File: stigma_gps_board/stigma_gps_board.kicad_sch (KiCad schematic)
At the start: 22 parts, among them J1 Conn_02x05_Top_Bottom, U1 NCP115AMX120TCG, U2 SAM-M10Q

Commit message: added 3d models and datasheets
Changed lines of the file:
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@@
 (kicad_sch
-	(version 20231120)
+	(version 20250114)
 	(generator "eeschema")
-	(generator_version "8.0")
+	(generator_version "9.0")
 	(paper "A4")
+	(rectangle
+		(start 128.27 59.69)
+		(end 189.23 95.25)
+		(stroke
+			(width 0)
+			(type default)
+		)
+		(fill
+			(type none)
+		)
+	)
+	(rectangle
+		(start 128.27 17.78)
+		(end 189.23 53.34)
+		(stroke
+			(width 0)
+			(type default)
+		)
+		(fill
+			(type none)
+		)
+	)
+	(rectangle
+		(start 128.27 99.06)
+		(end 189.23 132.08)
+		(stroke
+			(width 0)
+			(type default)
+		)
+		(fill
+			(type none)
+		)
+	)
+	(rectangle
+		(start 19.05 59.69)
+		(end 124.46 104.14)
+		(stroke
+			(width 0)
+			(type default)
+		)
+		(fill
+			(type none)
+		)
+	)
+	(rectangle
+		(start 19.05 17.78)
+		(end 124.46 53.34)
+		(stroke
+			(width 0)
+			(type default)
+		)
+		(fill
+			(type none)
+		)
+	)
+	(text "13mA should be the max. \nneeded current"
+		(exclude_from_sim no)
+		(at 110.998 101.092 0)
+		(effects
+			(font
+				(size 1.27 1.27)
+			)
+		)
+	)
+	(text "recomended chip setup"
+		(exclude_from_sim no)
+		(at 30.226 58.674 0)
+		(effects
+			(font
+				(size 1.27 1.27)
+			)
+		)
+	)
+	(text "connector and esd protection"
+		(exclude_from_sim no)
+		(at 33.274 16.51 0)
+		(effects
+			(font
+				(size 1.27 1.27)
+			)
+		)
+	)
+	(text "for more information about how to integrage refer to following:\nhttps://www.u-blox.com/en/product/sam-m10q-module?legacy=Current#Documentation-&-resources"
+		(exclude_from_sim no)
+		(at 19.05 107.188 0)
+		(effects
+			(font
+				(size 1.27 1.27)
+			)
+			(justify left)
+		)
+	)
+	(text "power supply\n"
+		(exclude_from_sim no)
+		(at 128.016 16.51 0)
+		(effects
+			(font
+				(size 1.27 1.27)
+			)
+			(justify left)
+		)
+	)
+	(text "todo: add footprint for connector (copy from stigma?)\n"
+		(exclude_from_sim no)
+		(at 47.244 55.372 0)
+		(effects
+			(font
+				(size 1.27 1.27)
+			)
+		)
+	)
+	(text "mounting hole m2"
+		(exclude_from_sim no)
+		(at 136.906 58.42 0)
+		(effects
+			(font
+				(size 1.27 1.27)
+			)
+		)
+	)
+	(text "mounting hole m4"
+		(exclude_from_sim no)
+		(at 136.906 98.044 0)
+		(effects
+			(font
+				(size 1.27 1.27)
+			)
+		)
+	)
 	(junction
 		(at 73.66 36.83)
@@
 		)
 	)
-	(rectangle
-		(start 128.27 59.69)
-		(end 189.23 95.25)
-		(stroke
-			(width 0)
-			(type default)
-		)
-		(fill
-			(type none)
-		)
-	)
-	(rectangle
-		(start 128.27 17.78)
-		(end 189.23 53.34)
-		(stroke
-			(width 0)
-			(type default)
-		)
-		(fill
-			(type none)
-		)
-	)
-	(rectangle
-		(start 128.27 99.06)
-		(end 189.23 132.08)
-		(stroke
-			(width 0)
-			(type default)
-		)
-		(fill
-			(type none)
-		)
-	)
-	(rectangle
-		(start 19.05 59.69)
-		(end 124.46 104.14)
-		(stroke
-			(width 0)
-			(type default)
-		)
-		(fill
-			(type none)
-		)
-	)
-	(rectangle
-		(start 19.05 17.78)
-		(end 124.46 53.34)
-		(stroke
-			(width 0)
-			(type default)
-		)
-		(fill
-			(type none)
-		)
-	)
-	(text "13mA should be the max. \nneeded current"
-		(exclude_from_sim no)
-		(at 110.998 101.092 0)
-		(effects
-			(font
-				(size 1.27 1.27)
-			)
-		)
-	)
-	(text "recomended chip setup"
-		(exclude_from_sim no)
-		(at 30.226 58.674 0)
-		(effects
-			(font
-				(size 1.27 1.27)
-			)
-		)
-	)
-	(text "connector and esd protection"
-		(exclude_from_sim no)
-		(at 33.274 16.51 0)
-		(effects
-			(font
-				(size 1.27 1.27)
-			)
-		)
-	)
-	(text "for more information about how to integrage refer to following:\nhttps://www.u-blox.com/en/product/sam-m10q-module?legacy=Current#Documentation-&-resources"
-		(exclude_from_sim no)
-		(at 19.05 107.188 0)
-		(effects
-			(font
-				(size 1.27 1.27)
-			)
-			(justify left)
-		)
-	)
-	(text "power supply\n"
-		(exclude_from_sim no)
-		(at 128.016 16.51 0)
-		(effects
-			(font
-				(size 1.27 1.27)
-			)
-			(justify left)
-		)
-	)
-	(text "todo: add footprint for connector (copy from stigma?)\n"
-		(exclude_from_sim no)
-		(at 47.244 55.372 0)
-		(effects
-			(font
-				(size 1.27 1.27)
-			)
-		)
-	)
-	(text "mounting hole m2"
-		(exclude_from_sim no)
-		(at 136.906 58.42 0)
-		(effects
-			(font
-				(size 1.27 1.27)
-			)
-		)
-	)
-	(text "mounting hole m4"
-		(exclude_from_sim no)
-		(at 136.906 98.044 0)
-		(effects
-			(font
-				(size 1.27 1.27)
-			)
-		)
-	)
 	(global_label "GPS_RESET"
 		(shape input)
@@
 		)
 	)
+	(embedded_fonts no)
 )

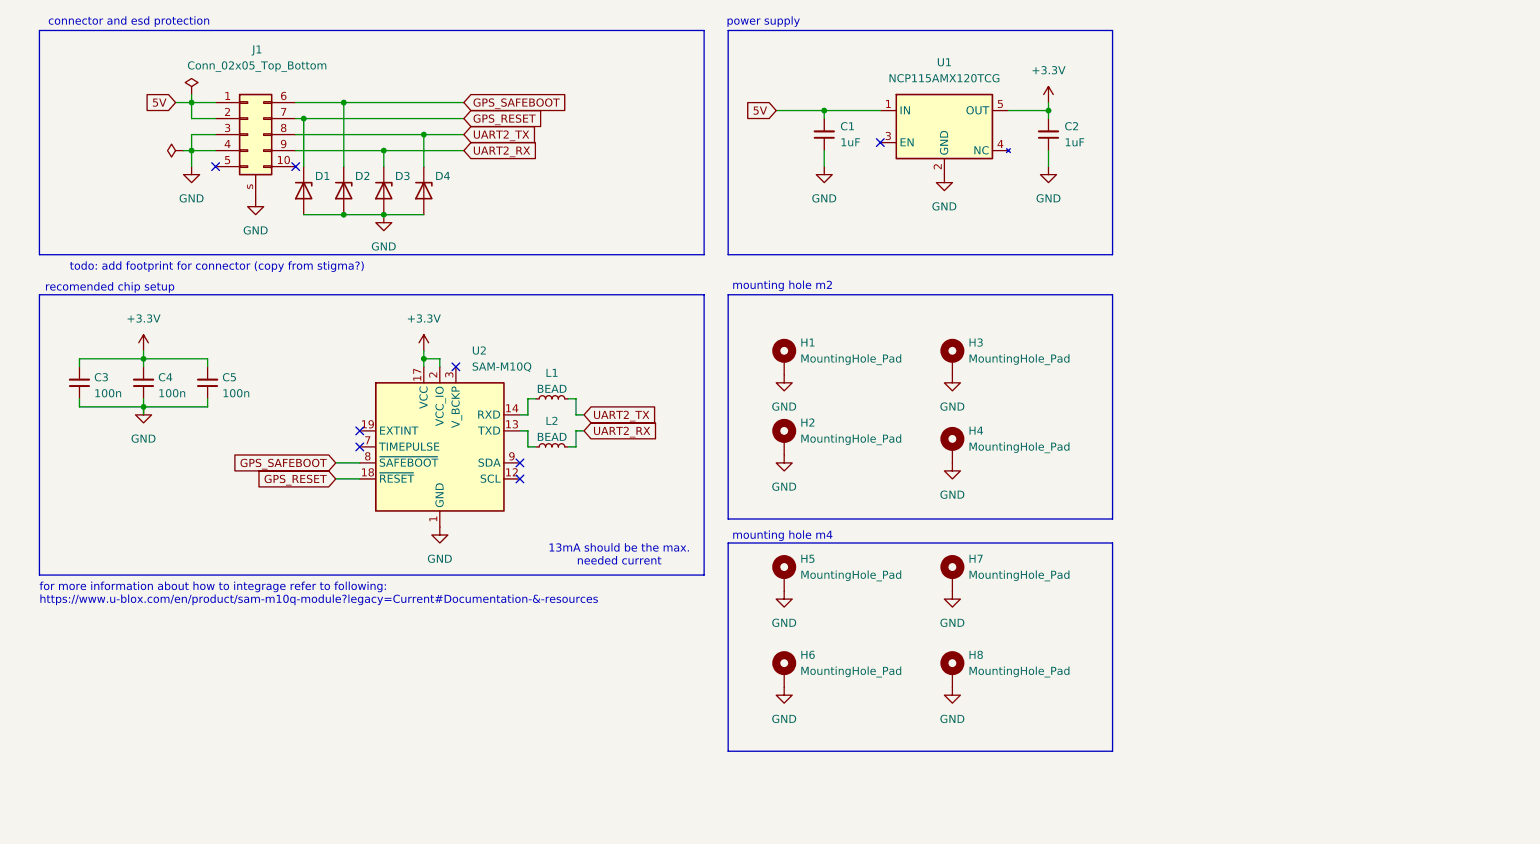
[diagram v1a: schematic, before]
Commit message: Update GPS board for mission board
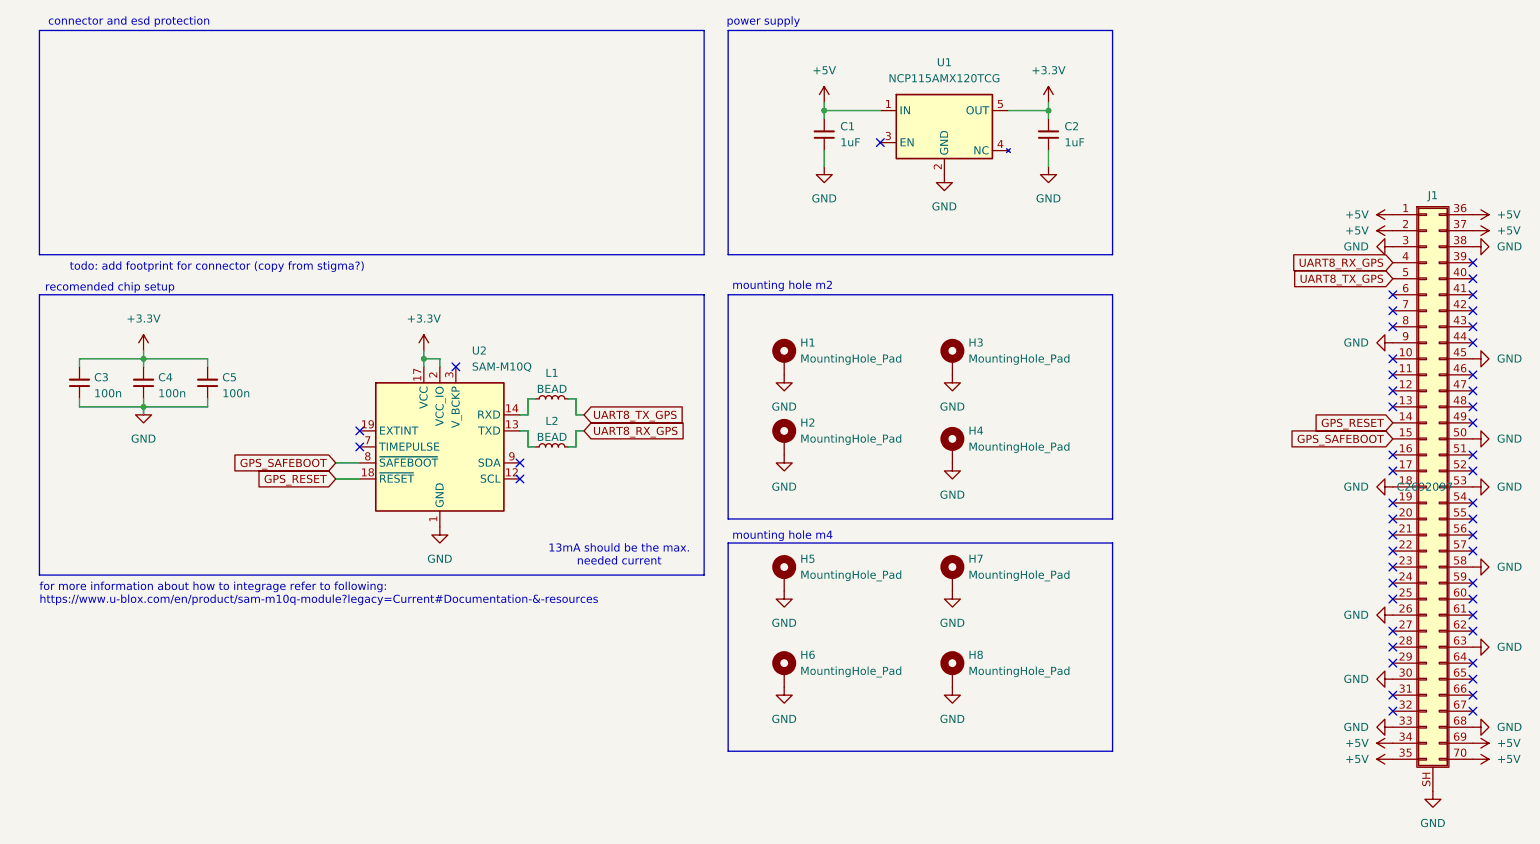
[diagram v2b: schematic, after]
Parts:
- removed D1, D2, D3, D4: ESD5Zxx, Diode_SMD:D_SOD-523, symbol Diode:ESD5Zxx
- removed J1: Conn_02x05_Top_Bottom, stigma:DF40GB-10DP-0.4V-plug, symbol Connector_Generic:Conn_02x05_Top_Bottom
- added J1: DF40GB-70DP-0.4V, stigma:DF40GB-70DP-0.4V-plug, symbol Connector_Generic_Shielded:Conn_02x35_Top_Bottom_Shielded
- H1, H2, H3, H4: footprint MountingHole:MountingHole_2.2mm_M2_DIN965_Pad_TopBottom -> MountingHole:MountingHole_2.2mm_M2_ISO14580_Pad
- H5, H6, H7, H8: footprint MountingHole:MountingHole_4.3mm_M4_DIN965_Pad_TopBottom -> MountingHole:MountingHole_4.3mm_M4_ISO14580_Pad
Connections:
- net GND: now also J1.18 (Pin_18), J1.26 (Pin_26), J1.3 (Pin_3), J1.30 (Pin_30), J1.33 (Pin_33), J1.38 (Pin_38), J1.45 (Pin_45), J1.50 (Pin_50), J1.53 (Pin_53), J1.58 (Pin_58), J1.63 (Pin_63), J1.68 (Pin_68), J1.9 (Pin_9), J1.SH (Shield)
- net GPS_RESET: now also J1.14 (Pin_14)
- net GPS_SAFEBOOT: now also J1.15 (Pin_15)
- net 5V renamed +5V
- net +5V: now also J1.1 (Pin_1), J1.2 (Pin_2), J1.34 (Pin_34), J1.35 (Pin_35), J1.36 (Pin_36), J1.37 (Pin_37), J1.69 (Pin_69), J1.70 (Pin_70)
- net UART2_RX renamed UART8_RX_GPS
- net UART8_RX_GPS: now also J1.4 (Pin_4)
- net UART2_TX renamed UART8_TX_GPS
- net UART8_TX_GPS: now also J1.5 (Pin_5)
- no-connect marks 8 -> 51

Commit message: Forgot to add in schematic
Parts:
- U1: LCSC (none) -> C603505
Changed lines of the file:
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@@
 			)
 		)
-		(property "Datasheet" "chrome-extension://efaidnbmnnnibpcajpcglclefindmkaj/https://www.mouser.de/datasheet/2/308/1/NCP115_D-3366525.pdf"
+		(property "Datasheet" "https://www.mouser.de/datasheet/2/308/1/NCP115_D-3366525.pdf"
 			(at 162.56 33.02 0)
 			(effects
@@
 			(at 162.56 33.02 0)
 			(effects
+				(font
+					(size 1.27 1.27)
+				)
+				(hide yes)
+			)
+		)
+		(property "LCSC" "C603505"
+			(at 162.56 33.02 0)
+			(effects

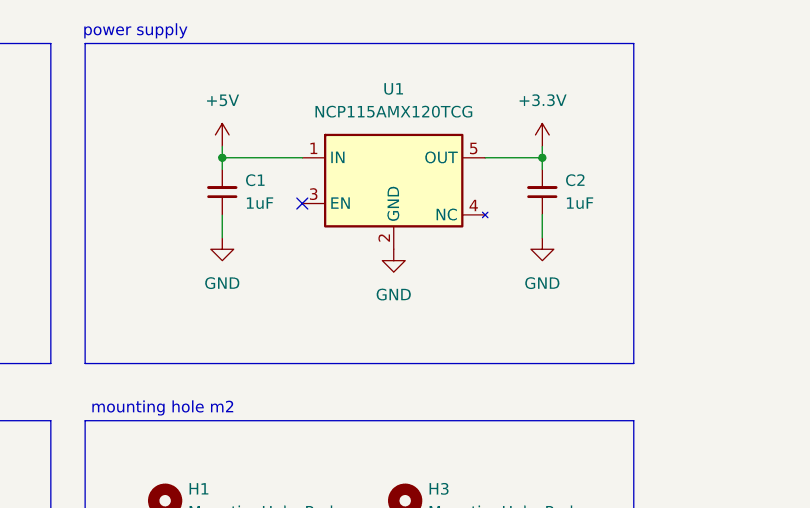
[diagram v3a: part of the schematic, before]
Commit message: fix voltage regulator
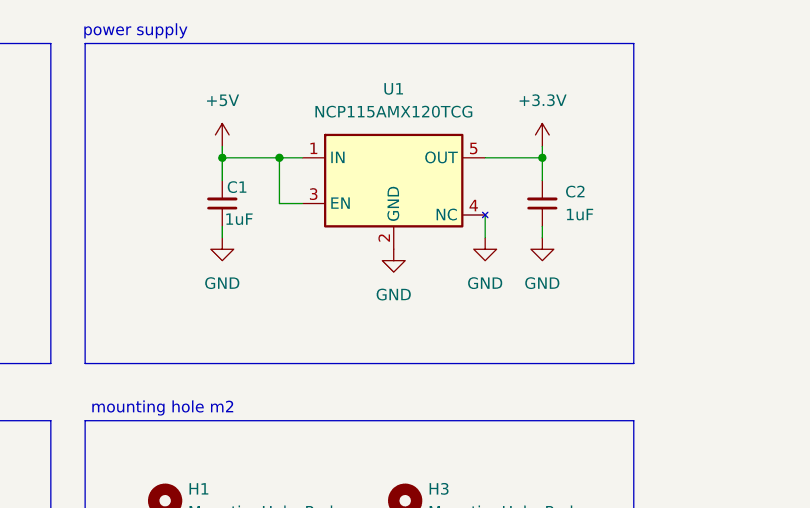
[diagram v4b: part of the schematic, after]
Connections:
- net +5V: now also U1.3 (EN)
- net GND: now also U1.4 (NC)
- no-connect marks 51 -> 50
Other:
- moved on the sheet: C1, C2
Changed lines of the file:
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@@
 		(color 0 0 0 0)
 	)
+	(junction
+		(at 149.86 30.48)
+		(diameter 0)
+		(color 0 0 0 0)
+	)
 	(no_connect
 		(at 246.38 54.61)
@@
 	)
 	(no_connect
-		(at 152.4 35.56)
-	)
-	(no_connect
 		(at 85.09 71.12)
 	)
@@
 	(wire
 		(pts
-			(xy 179.07 30.48) (xy 179.07 31.75)
+			(xy 179.07 30.48) (xy 179.07 33.02)
 		)
 		(stroke
@@
 	(wire
 		(pts
-			(xy 143.51 30.48) (xy 152.4 30.48)
+			(xy 143.51 30.48) (xy 149.86 30.48)
 		)
 		(stroke
@@
 	(wire
 		(pts
-			(xy 143.51 36.83) (xy 143.51 39.37)
+			(xy 143.51 38.1) (xy 143.51 39.37)
 		)
 		(stroke
@@
 	(wire
 		(pts
-			(xy 143.51 30.48) (xy 143.51 31.75)
+			(xy 143.51 30.48) (xy 143.51 33.02)
 		)
 		(stroke
@@
 	(wire
 		(pts
-			(xy 179.07 36.83) (xy 179.07 39.37)
+			(xy 179.07 38.1) (xy 179.07 39.37)
 		)
 		(stroke
@@
 	(wire
 		(pts
+			(xy 149.86 35.56) (xy 149.86 30.48)
+		)
+		(stroke
+			(width 0)
+			(type default)
+		)
+	)
+	(wire
+		(pts
 			(xy 104.14 76.2) (xy 104.14 78.74)
 		)
@@
 	(wire
 		(pts
+			(xy 149.86 35.56) (xy 152.4 35.56)
+		)
+		(stroke
+			(width 0)
+			(type default)
+		)
+	)
+	(wire
+		(pts
+			(xy 172.72 36.83) (xy 172.72 39.37)
+		)
+		(stroke
+			(width 0)
+			(type default)
+		)
+	)
+	(wire
+		(pts
 			(xy 102.87 83.82) (xy 104.14 83.82)
 		)
@@
 	(wire
 		(pts
+			(xy 149.86 30.48) (xy 152.4 30.48)
+		)
+		(stroke
+			(width 0)
+			(type default)
+		)
+	)
+	(wire
+		(pts
 			(xy 66.04 86.36) (xy 69.85 86.36)
 		)
@@
 	(symbol
 		(lib_id "Device:C_Small")
-		(at 179.07 34.29 180)
+		(at 179.07 35.56 180)
 		(unit 1)
 		(exclude_from_sim no)
@@
 		(fields_autoplaced yes)
 		(property "Reference" "C2"
-			(at 181.61 33.0135 0)
+			(at 181.61 34.2835 0)
 			(effects
 				(font
@@
 		)
 		(property "Value" "1uF"
-			(at 181.61 35.5535 0)
+			(at 181.61 36.8235 0)
 			(effects
 				(font
@@
 		)
 		(property "Footprint" "Capacitor_SMD:C_0603_1608Metric_Pad1.08x0.95mm_HandSolder"
-			(at 179.07 34.29 0)
+			(at 179.07 35.56 0)
 			(effects
 				(font
@@
 		)
 		(property "Datasheet" "~"
-			(at 179.07 34.29 0)
+			(at 179.07 35.56 0)
 			(effects
 				(font
@@
 		)
 		(property "Description" ""
-			(at 179.07 34.29 0)
+			(at 179.07 35.56 0)
 			(effects
 				(font
@@
 		)
 		(property "LCSC#" "C1591"
-			(at 179.07 34.29 0)
+			(at 179.07 35.56 0)
 			(effects
 				(font
@@
 		)
 		(property "Manufacturer" "Samsung Electro-Mechanics"
-			(at 179.07 34.29 0)
+			(at 179.07 35.56 0)
 			(effects
 				(font
@@
 		)
 		(property "Part#" "CL10B104KB8NNNC"
-			(at 179.07 34.29 0)
+			(at 179.07 35.56 0)
 			(effects
 				(font
@@
 	)
 	(symbol
-		(lib_id "Device:C_Small")
-		(at 143.51 34.29 180)
+		(lib_id "power:GND")
+		(at 172.72 39.37 0)
 		(unit 1)
 		(exclude_from_sim no)
@@
 		(dnp no)
 		(fields_autoplaced yes)
+		(property "Reference" "#PWR02"
+			(at 172.72 45.72 0)
+			(effects
+				(font
+					(size 1.27 1.27)
+				)
+				(hide yes)
+			)
+		)
+		(property "Value" "GND"
+			(at 172.72 44.45 0)
+			(effects
+				(font
+					(size 1.27 1.27)
+				)
+			)
+		)
+		(property "Footprint" ""
+			(at 172.72 39.37 0)
+			(effects
+				(font
+					(size 1.27 1.27)
+				)
+				(hide yes)
+			)
+		)
+		(property "Datasheet" ""
+			(at 172.72 39.37 0)
+			(effects
+				(font
+					(size 1.27 1.27)
+				)
+				(hide yes)
+			)
+		)
+		(property "Description" "Power symbol creates a global label with name \"GND\" , ground"
+			(at 172.72 39.37 0)
+			(effects
+				(font
+					(size 1.27 1.27)
+				)
+				(hide yes)
+			)
+		)
+		(pin "1"
+		)
+		(instances
+			(project "stigma_gps_board"
+				(path "/9327cffc-7a3b-415d-89e5-7d37bd09d58e"
+					(reference "#PWR02")
+					(unit 1)
+				)
+			)
+		)
+	)
+	(symbol
+		(lib_id "Device:C_Small")
+		(at 143.51 35.56 180)
+		(unit 1)
+		(exclude_from_sim no)
+		(in_bom yes)
+		(on_board yes)
+		(dnp no)
 		(property "Reference" "C1"
-			(at 146.05 33.0135 0)
+			(at 144.018 33.782 0)
 			(effects
 				(font
@@
 		)
 		(property "Value" "1uF"
-			(at 146.05 35.5535 0)
+			(at 143.764 37.338 0)
 			(effects
 				(font
@@
 		)
 		(property "Footprint" "Capacitor_SMD:C_0603_1608Metric_Pad1.08x0.95mm_HandSolder"
-			(at 143.51 34.29 0)
+			(at 143.51 35.56 0)
 			(effects
 				(font
@@
 		)
 		(property "Datasheet" "~"
-			(at 143.51 34.29 0)
+			(at 143.51 35.56 0)
 			(effects
 				(font
@@
 		)
 		(property "Description" ""
-			(at 143.51 34.29 0)
+			(at 143.51 35.56 0)
 			(effects
 				(font
@@
 		)
 		(property "LCSC#" "C1591"
-			(at 143.51 34.29 0)
+			(at 143.51 35.56 0)
 			(effects
 				(font
@@
 		)
 		(property "Manufacturer" "Samsung Electro-Mechanics"
-			(at 143.51 34.29 0)
+			(at 143.51 35.56 0)
 			(effects
 				(font
@@
 		)
 		(property "Part#" "CL10B104KB8NNNC"
-			(at 143.51 34.29 0)
+			(at 143.51 35.56 0)
 			(effects
 				(font
